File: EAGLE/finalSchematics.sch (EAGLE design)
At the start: 8 parts, among them IC1 STM32F103RBT, Q1 8MHz 131-220

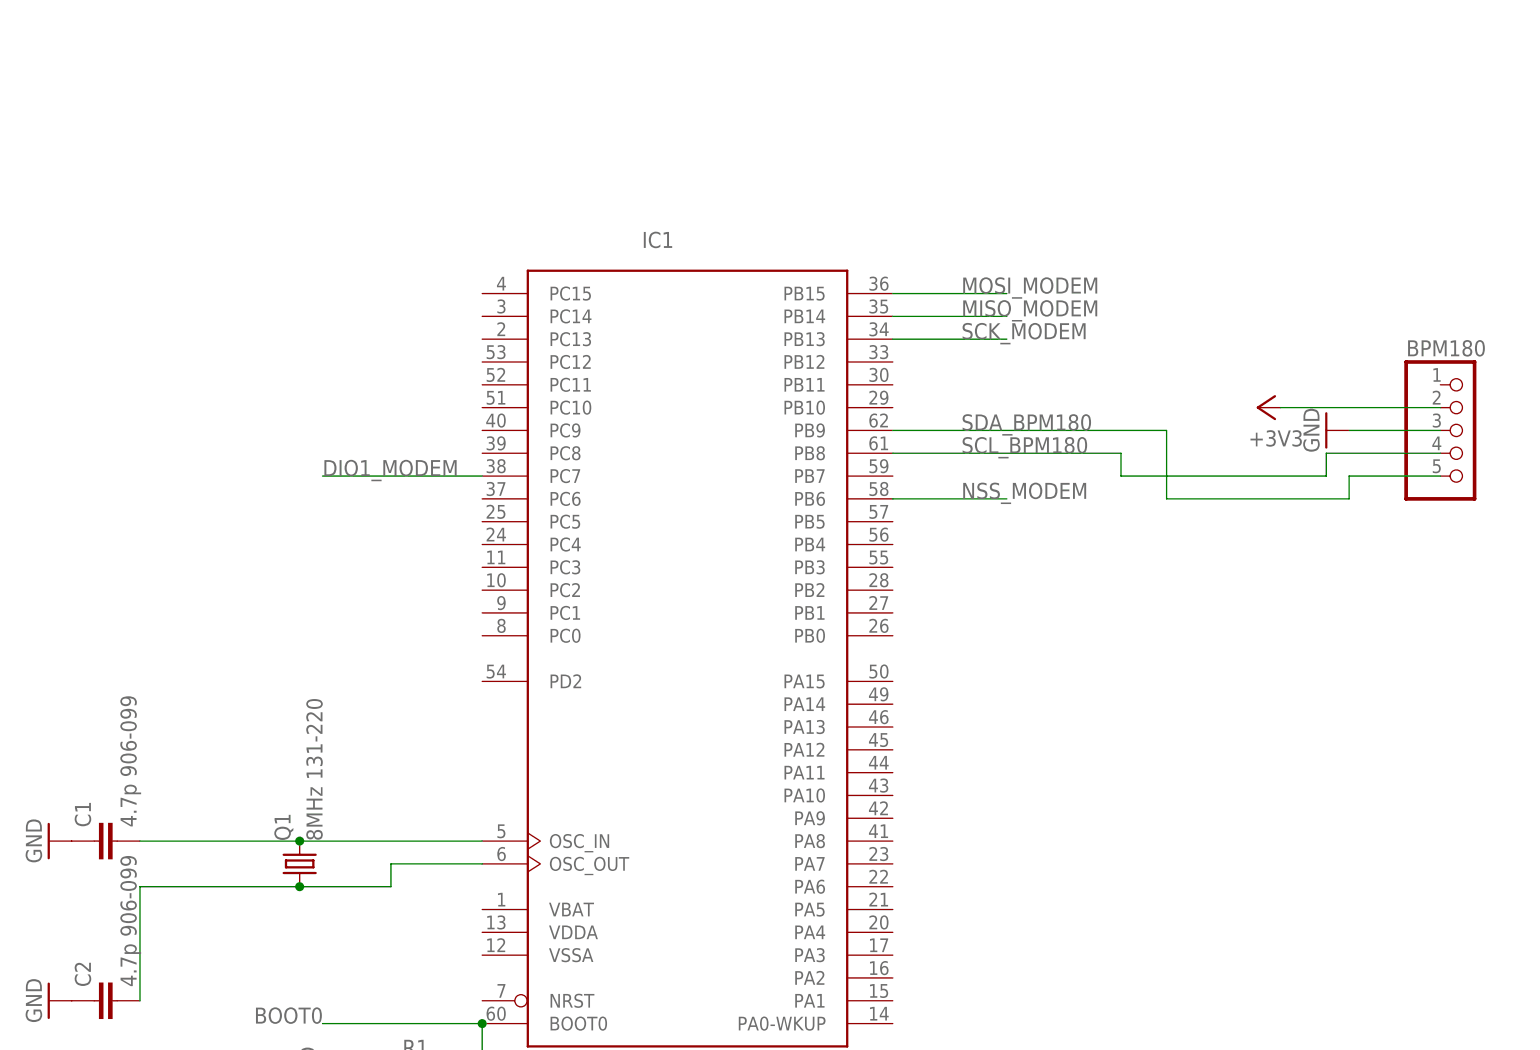
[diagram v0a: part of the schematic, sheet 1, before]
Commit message: Eagle file ready for meeting with Vojta S.
Missing GPS module footer. Our module is L70 and only L80 library was
found. Will have to resolve later by creating a library at Mucirna.

Repositories folder updated with new documentation
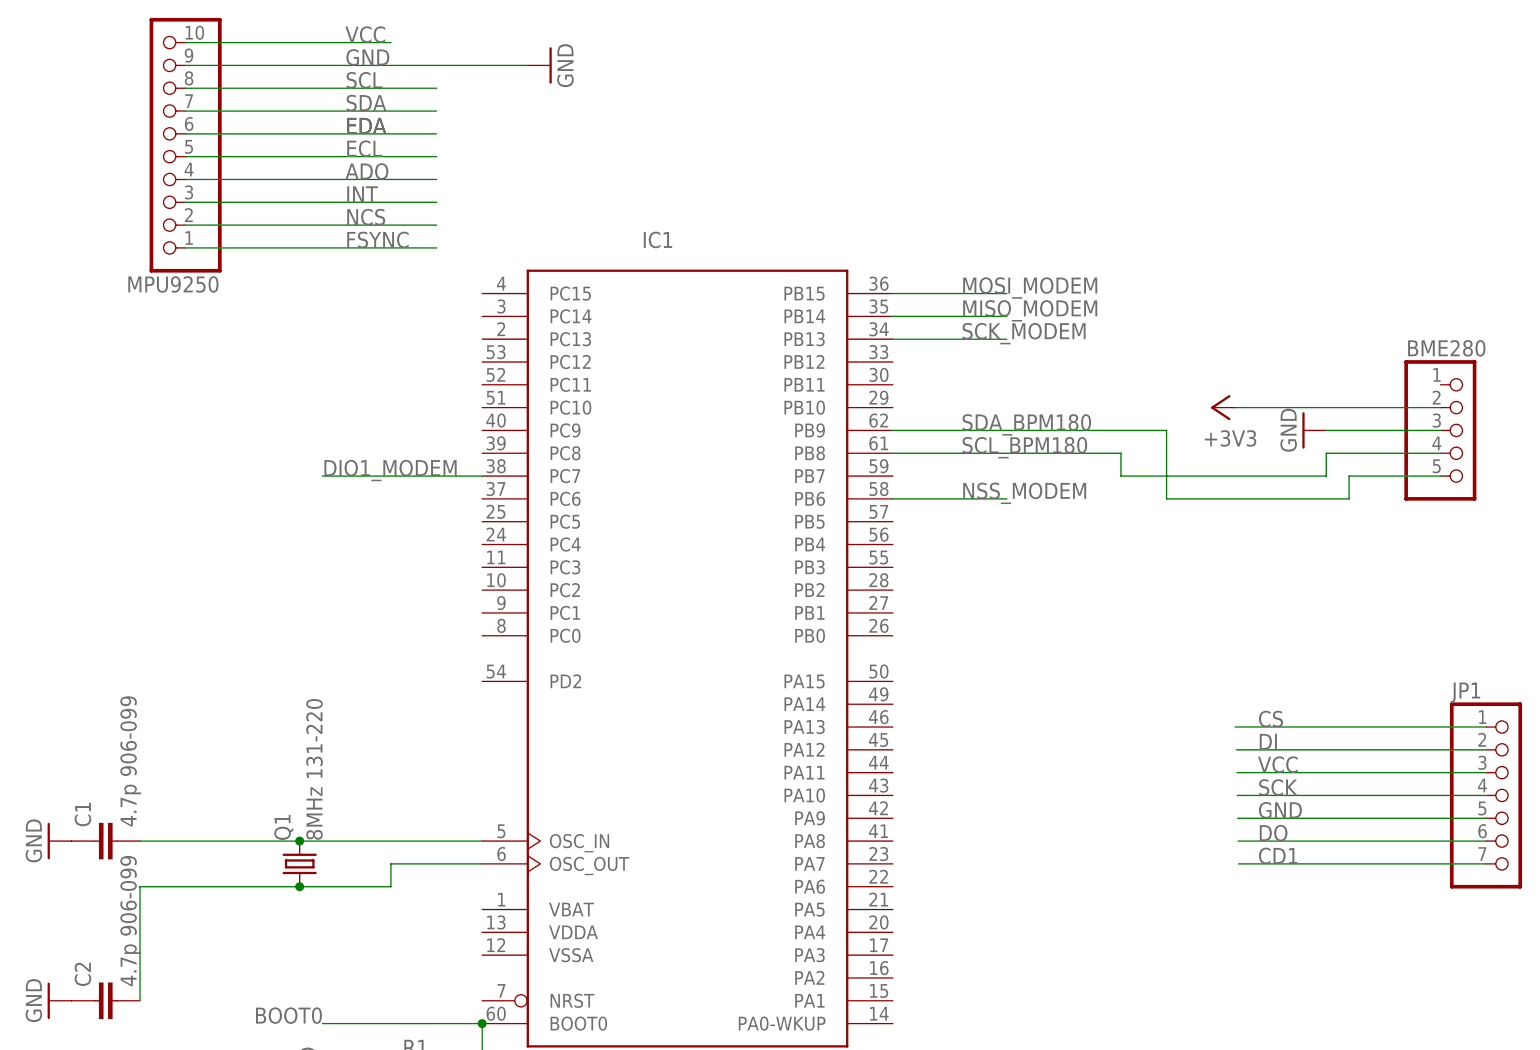
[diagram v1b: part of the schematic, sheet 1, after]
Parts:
- added GPSANA: ANT-NSG4712-6, roundsolutions:ANT-NSG4712-6
- added JP1: (no value), pinhead:PINHD-1X7
- added MPU9250: (no value), pinhead:PINHD-1X10
- renumbered ANT1 to RADIOANA, BPM180 to BME280
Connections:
- new net ADO: MPU9250.4
- new net CD1: JP1.7
- new net CS: JP1.1
- new net DI: JP1.2
- new net DO: JP1.6
- new net ECL: MPU9250.5
- new net EDA: MPU9250.6
- new net FSYNC: MPU9250.1
- new net INT: MPU9250.3
- new net NCS: MPU9250.2
- new net SCK: JP1.4
- new net SCL: MPU9250.8
- new net SDA: MPU9250.7
- new net VCC: JP1.3, MPU9250.10
- net GND: now also JP1.5, MPU9250.9
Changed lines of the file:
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@@
 <layers>
 <layer number="1" name="Top" color="4" fill="1" visible="no" active="no"/>
+<layer number="2" name="Route2" color="1" fill="3" visible="no" active="no"/>
+<layer number="3" name="Route3" color="4" fill="3" visible="no" active="no"/>
+<layer number="4" name="Route4" color="1" fill="4" visible="no" active="no"/>
+<layer number="5" name="Route5" color="4" fill="4" visible="no" active="no"/>
+<layer number="6" name="Route6" color="1" fill="8" visible="no" active="no"/>
+<layer number="7" name="Route7" color="4" fill="8" visible="no" active="no"/>
+<layer number="8" name="Route8" color="1" fill="2" visible="no" active="no"/>
+<layer number="9" name="Route9" color="4" fill="2" visible="no" active="no"/>
+<layer number="10" name="Route10" color="1" fill="7" visible="no" active="no"/>
+<layer number="11" name="Route11" color="4" fill="7" visible="no" active="no"/>
+<layer number="12" name="Route12" color="1" fill="5" visible="no" active="no"/>
+<layer number="13" name="Route13" color="4" fill="5" visible="no" active="no"/>
+<layer number="14" name="Route14" color="1" fill="6" visible="no" active="no"/>
+<layer number="15" name="Route15" color="4" fill="6" visible="no" active="no"/>
 <layer number="16" name="Bottom" color="1" fill="1" visible="no" active="no"/>
 <layer number="17" name="Pads" color="2" fill="1" visible="no" active="no"/>
@@
 <part name="U$1" library="RFM69mod" deviceset="RFM69" device=""/>
 <part name="GND4" library="supply1" deviceset="GND" device=""/>
-<part name="ANT1" library="discrete" deviceset="ANTENNA" device=""/>
+<part name="RADIOANA" library="discrete" deviceset="ANTENNA" device=""/>
 <part name="+3V1" library="supply1" deviceset="+3V3" device=""/>
-<part name="BPM180" library="pinhead" deviceset="PINHD-1X5" device="/90"/>
+<part name="BME280" library="pinhead" deviceset="PINHD-1X5" device="/90"/>
 <part name="+3V2" library="supply1" deviceset="+3V3" device=""/>
 <part name="GND5" library="supply1" deviceset="GND" device=""/>
+<part name="MPU9250" library="pinhead" deviceset="PINHD-1X10" device=""/>
+<part name="GND6" library="supply1" deviceset="GND" device=""/>
+<part name="JP1" library="pinhead" deviceset="PINHD-1X7" device=""/>
+<part name="GPSANA" library="roundsolutions" deviceset="ANT-NSG4712-6" device=""/>
 </parts>
 <sheets>
@@
 <instance part="R1" gate="G$1" x="45.72" y="7.62"/>
 <instance part="GND3" gate="1" x="33.02" y="7.62" rot="R270"/>
-<instance part="BPM180" gate="A" x="160.02" y="78.74"/>
-<instance part="+3V2" gate="G$1" x="137.16" y="81.28" rot="R90"/>
-<instance part="GND5" gate="1" x="144.78" y="78.74" rot="R270"/>
+<instance part="BME280" gate="A" x="160.02" y="78.74"/>
+<instance part="+3V2" gate="G$1" x="132.08" y="81.28" rot="R90"/>
+<instance part="GND5" gate="1" x="142.24" y="78.74" rot="R270"/>
+<instance part="MPU9250" gate="A" x="15.24" y="109.22" rot="R180"/>
+<instance part="GND6" gate="1" x="58.42" y="119.38" rot="R90"/>
+<instance part="JP1" gate="A" x="165.1" y="38.1"/>
 </instances>
 <busses>
@@
 </segment>
 <segment>
-<pinref part="BPM180" gate="A" pin="3"/>
-<wire x1="157.48" y1="78.74" x2="147.32" y2="78.74" width="0.1524" layer="91"/>
+<pinref part="BME280" gate="A" pin="3"/>
+<wire x1="157.48" y1="78.74" x2="144.78" y2="78.74" width="0.1524" layer="91"/>
 <pinref part="GND5" gate="1" pin="GND"/>
+</segment>
+<segment>
+<pinref part="MPU9250" gate="A" pin="9"/>
+<wire x1="17.78" y1="119.38" x2="55.88" y2="119.38" width="0.1524" layer="91"/>
+<label x="35.56" y="119.38" size="1.778" layer="95"/>
+<pinref part="GND6" gate="1" pin="GND"/>
+</segment>
+<segment>
+<pinref part="JP1" gate="A" pin="5"/>
+<wire x1="162.56" y1="35.56" x2="134.91543125" y2="35.56" width="0.1524" layer="91"/>
+<label x="137.16" y="35.56" size="1.778" layer="95"/>
 </segment>
 </net>
@@
 <pinref part="IC1" gate="MCU" pin="PB8"/>
 <label x="104.14" y="76.2" size="1.778" layer="95"/>
-<pinref part="BPM180" gate="A" pin="4"/>
+<pinref part="BME280" gate="A" pin="4"/>
 <wire x1="157.48" y1="76.2" x2="144.78" y2="76.2" width="0.1524" layer="91"/>
 <wire x1="144.78" y1="76.2" x2="144.78" y2="73.66" width="0.1524" layer="91"/>
@@
 <pinref part="IC1" gate="MCU" pin="PB9"/>
 <label x="104.14" y="78.74" size="1.778" layer="95"/>
-<pinref part="BPM180" gate="A" pin="5"/>
+<pinref part="BME280" gate="A" pin="5"/>
 <wire x1="157.48" y1="73.66" x2="147.32" y2="73.66" width="0.1524" layer="91"/>
 <wire x1="147.32" y1="73.66" x2="147.32" y2="71.12" width="0.1524" layer="91"/>
@@
 <net name="+3V3" class="0">
 <segment>
-<pinref part="BPM180" gate="A" pin="2"/>
-<wire x1="157.48" y1="81.28" x2="139.7" y2="81.28" width="0.1524" layer="91"/>
+<pinref part="BME280" gate="A" pin="2"/>
+<wire x1="157.48" y1="81.28" x2="134.62" y2="81.28" width="0.1524" layer="91"/>
 <pinref part="+3V2" gate="G$1" pin="+3V3"/>
+</segment>
+</net>
+<net name="VCC" class="0">
+<segment>
+<pinref part="MPU9250" gate="A" pin="10"/>
+<wire x1="17.78" y1="121.92" x2="40.64" y2="121.92" width="0.1524" layer="91"/>
+<label x="35.56" y="121.92" size="1.778" layer="95"/>
+</segment>
+<segment>
+<pinref part="JP1" gate="A" pin="3"/>
+<wire x1="162.56" y1="40.64" x2="134.818734375" y2="40.64" width="0.1524" layer="91"/>
+<label x="137.16" y="40.64" size="1.778" layer="95"/>
+</segment>
+</net>
+<net name="SCL" class="0">
+<segment>
+<pinref part="MPU9250" gate="A" pin="8"/>
+<wire x1="17.78" y1="116.84" x2="45.72" y2="116.84" width="0.1524" layer="91"/>
+<label x="35.56" y="116.84" size="1.778" layer="95"/>
+</segment>
+</net>
+<net name="SDA" class="0">
+<segment>
+<pinref part="MPU9250" gate="A" pin="7"/>
+<wire x1="17.78" y1="114.3" x2="45.72" y2="114.3" width="0.1524" layer="91"/>
+<label x="35.56" y="114.3" size="1.778" layer="95"/>
+</segment>
+</net>
+<net name="EDA" class="0">
+<segment>
+<pinref part="MPU9250" gate="A" pin="6"/>
+<wire x1="17.78" y1="111.76" x2="45.72" y2="111.76" width="0.1524" layer="91"/>
+<label x="35.56" y="111.76" size="1.778" layer="95"/>
+<label x="35.56" y="111.76" size="1.778" layer="95"/>
+</segment>
+</net>
+<net name="ECL" class="0">
+<segment>
+<pinref part="MPU9250" gate="A" pin="5"/>
+<wire x1="17.78" y1="109.22" x2="45.72" y2="109.22" width="0.1524" layer="91"/>
+<label x="35.56" y="109.22" size="1.778" layer="95"/>
+</segment>
+</net>
+<net name="ADO" class="0">
+<segment>
+<pinref part="MPU9250" gate="A" pin="4"/>
+<wire x1="17.78" y1="106.68" x2="45.72" y2="106.68" width="0.1524" layer="91"/>
+<label x="35.56" y="106.68" size="1.778" layer="95"/>
+</segment>
+</net>
+<net name="INT" class="0">
+<segment>
+<pinref part="MPU9250" gate="A" pin="3"/>
+<wire x1="17.78" y1="104.14" x2="45.72" y2="104.14" width="0.1524" layer="91"/>
+<label x="35.56" y="104.14" size="1.778" layer="95"/>
+</segment>
+</net>
+<net name="NCS" class="0">
+<segment>
+<pinref part="MPU9250" gate="A" pin="2"/>
+<wire x1="17.78" y1="101.6" x2="45.72" y2="101.6" width="0.1524" layer="91"/>
+<label x="35.56" y="101.6" size="1.778" layer="95"/>
+</segment>
+</net>
+<net name="FSYNC" class="0">
+<segment>
+<pinref part="MPU9250" gate="A" pin="1"/>
+<wire x1="17.78" y1="99.06" x2="45.72" y2="99.06" width="0.1524" layer="91"/>
+<label x="35.56" y="99.06" size="1.778" layer="95"/>
+</segment>
+</net>
+<net name="CS" class="0">
+<segment>
+<pinref part="JP1" gate="A" pin="1"/>
+<wire x1="162.56" y1="45.72" x2="134.62" y2="45.72" width="0.1524" layer="91"/>
+<label x="137.16" y="45.72" size="1.778" layer="95"/>
+</segment>
+</net>
+<net name="DI" class="0">
+<segment>
+<pinref part="JP1" gate="A" pin="2"/>
+<wire x1="162.56" y1="43.18" x2="134.7703875" y2="43.18" width="0.1524" layer="91"/>
+<label x="137.16" y="43.18" size="1.778" layer="95"/>
+</segment>
+</net>
+<net name="SCK" class="0">
+<segment>
+<pinref part="JP1" gate="A" pin="4"/>
+<wire x1="162.56" y1="38.1" x2="134.86708125" y2="38.1" width="0.1524" layer="91"/>
+<label x="137.16" y="38.1" size="1.778" layer="95"/>
+</segment>
+</net>
+<net name="DO" class="0">
+<segment>
+<pinref part="JP1" gate="A" pin="6"/>
+<wire x1="162.56" y1="33.02" x2="134.963778125" y2="33.02" width="0.1524" layer="91"/>
+<label x="137.16" y="33.02" size="1.778" layer="95"/>
+</segment>
+</net>
+<net name="CD1" class="0">
+<segment>
+<pinref part="JP1" gate="A" pin="7"/>
+<wire x1="162.56" y1="30.48" x2="135.012125" y2="30.48" width="0.1524" layer="91"/>
+<label x="137.16" y="30.48" size="1.778" layer="95"/>
 </segment>
 </net>
@@
 <instance part="U$1" gate="G$1" x="114.3" y="88.9"/>
 <instance part="GND4" gate="1" x="134.62" y="86.36"/>
-<instance part="ANT1" gate="A" x="142.24" y="93.98" rot="R270"/>
+<instance part="RADIOANA" gate="A" x="142.24" y="93.98" rot="R270"/>
 <instance part="+3V1" gate="G$1" x="53.34" y="91.44" rot="R90"/>
+<instance part="GPSANA" gate="G$1" x="165.1" y="152.4"/>
 </instances>
 <busses>
@@
 <pinref part="U$1" gate="G$1" pin="ANA"/>
 <wire x1="109.22" y1="93.98" x2="137.16" y2="93.98" width="0.1524" layer="91"/>
-<pinref part="ANT1" gate="A" pin="1"/>
-</segment>
-</net>
+<pinref part="RADIOANA" gate="A" pin="1"/>
+</segment>
+</net>
